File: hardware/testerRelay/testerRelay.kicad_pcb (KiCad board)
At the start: 2 copper layers, 100 x 70 mm, 12 parts, among them J21 relay, J22 relay, J70 transformer, J71 PM9808_L, J72 actuator, K10 HF115-005-2ZS4, K11 HF115-005-2ZS4, K12 HF115-005-2ZS4, K13 HF115-005-2ZS4, K14 HF115-005-2ZS4, K15 HF115-005-2ZS4, K16 HF115-005-2ZS4

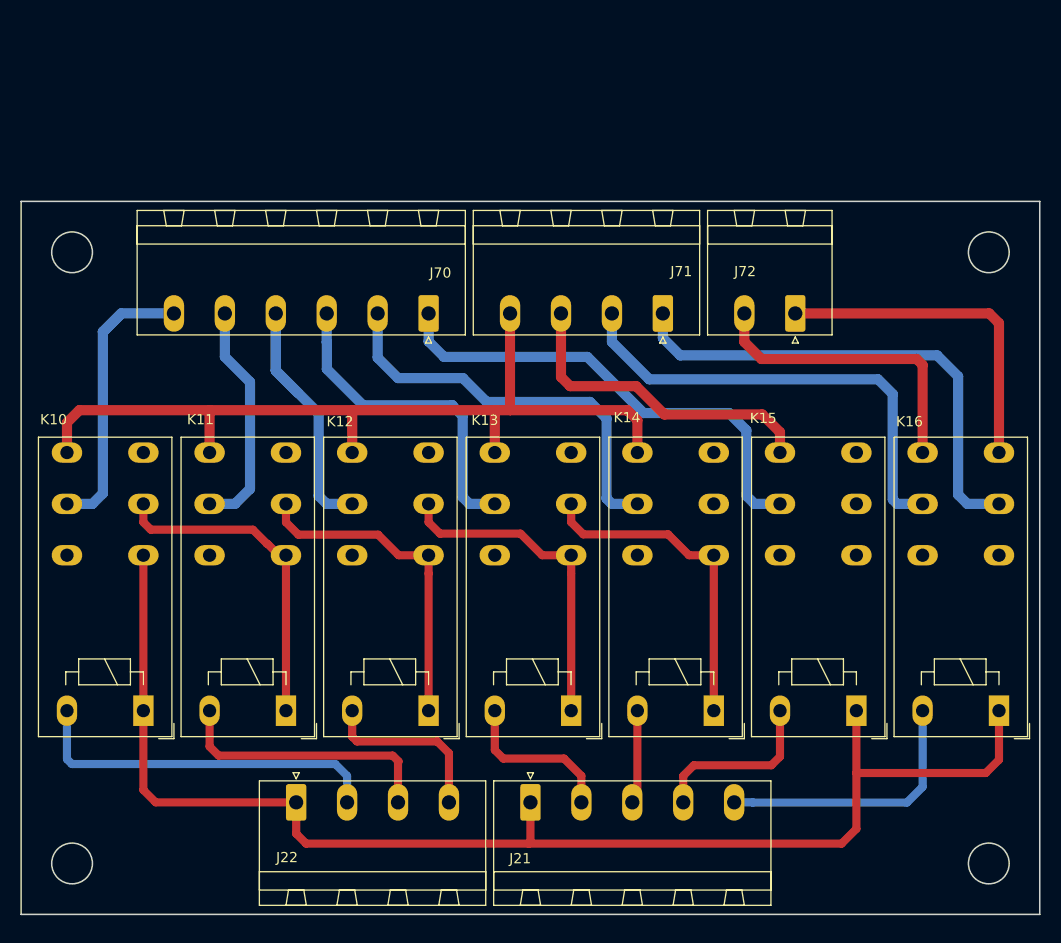
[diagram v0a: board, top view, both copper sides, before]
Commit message: adjustment line direction
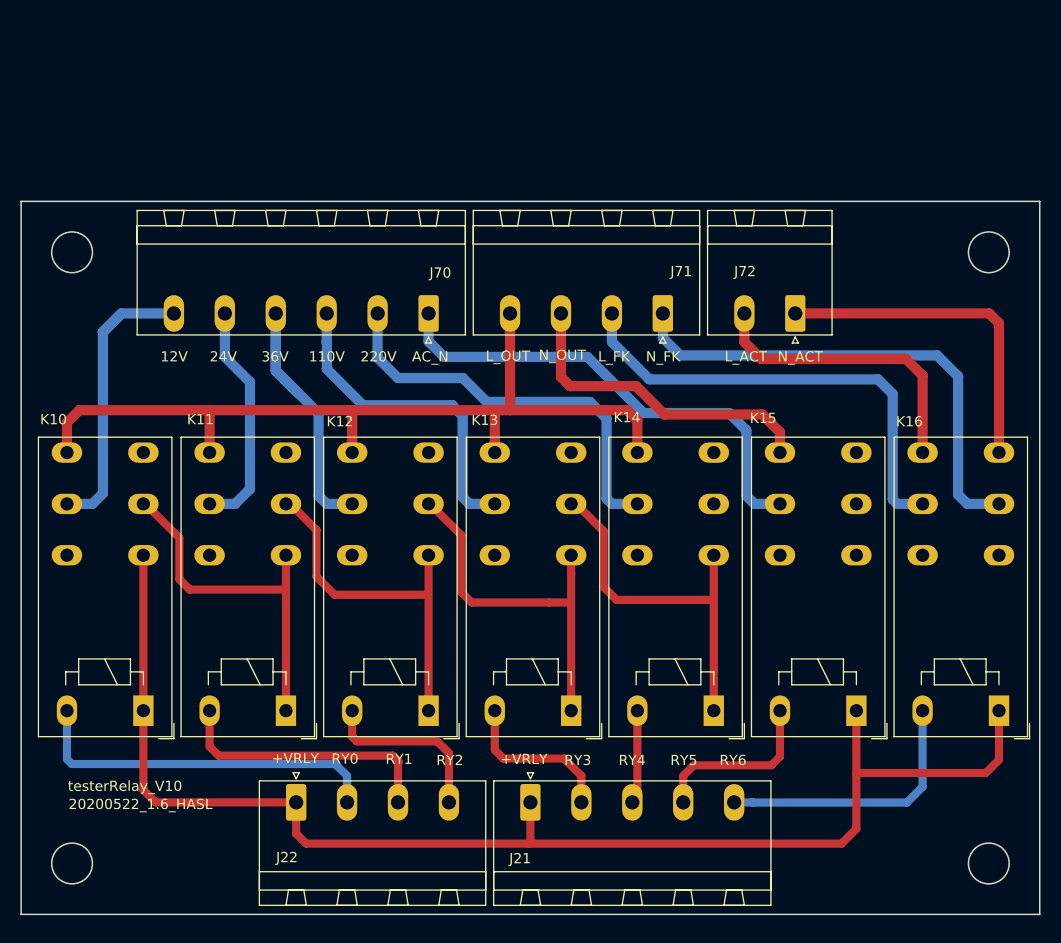
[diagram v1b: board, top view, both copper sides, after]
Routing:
- net /K13CV: track 32.4 -> 36.2 mm
- net /K14CV: track 32.4 -> 36.0 mm
- net /K12CV: track 32.4 -> 35.5 mm
- net /K11CV: track 32.4 -> 35.1 mm
- net /L_ACT: track 29.8 -> 29.2 mm
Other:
- board text added: "+VRLY"
- board text added: "110V"
- board text added: "12V"
- board text added: "20200522_1.6_HASL"
- board text added: "220V"
- board text added: "24V"
- board text added: "36V"
- board text added: "AC_N"
- board text added: "L_ACT"
- board text added: "L_FK"
- board text added: "L_OUT"
- board text added: "N_ACT"
- board text added: "N_FK"
- board text added: "N_OUT"
- board text added: "RY0"
- board text added: "RY1"
- board text added: "RY2"
- board text added: "RY3"
- board text added: "RY4"
- board text added: "RY5"
- board text added: "RY6"
- board text added: "testerRelay_V10"
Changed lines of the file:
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@@
   (general
     (thickness 1.6)
-    (drawings 8)
-    (tracks 181)
+    (drawings 31)
+    (tracks 179)
     (zones 0)
     (modules 12)
@@
     (pad_to_mask_clearance 0)
     (aux_axis_origin 0 0)
-    (visible_elements FFFFFF7F)
+    (visible_elements 7FFFFFFF)
     (pcbplotparams
       (layerselection 0x010fc_ffffffff)
@@
       (outputformat 1)
       (mirror false)
-      (drillshape 1)
+      (drillshape 0)
       (scaleselection 1)
-      (outputdirectory ""))
+      (outputdirectory "testerRelay_V10"))
   )
   (net 0 "")
@@
       (rotate (xyz 0 0 0))
     )
+  )
+  (gr_text 20200522_1.6_HASL (at 61.722 139.192) (layer F.SilkS)
+    (effects (font (size 1 1) (thickness 0.2)))
+  )
+  (gr_text testerRelay_V10 (at 60.198 137.414) (layer F.SilkS)
+    (effects (font (size 1 1) (thickness 0.2)))
+  )
+  (gr_text N_ACT (at 126.492 95.25) (layer F.SilkS)
+    (effects (font (size 1 1) (thickness 0.2)))
+  )
+  (gr_text L_ACT (at 121.158 95.25) (layer F.SilkS)
+    (effects (font (size 1 1) (thickness 0.2)))
+  )
+  (gr_text N_FK (at 113.03 95.25) (layer F.SilkS)
+    (effects (font (size 1 1) (thickness 0.2)))
+  )
+  (gr_text L_FK (at 108.204 95.25) (layer F.SilkS)
+    (effects (font (size 1 1) (thickness 0.2)))
+  )
+  (gr_text N_OUT (at 103.124 95.1) (layer F.SilkS)
+    (effects (font (size 1 1) (thickness 0.2)))
+  )
+  (gr_text L_OUT (at 97.79 95.19) (layer F.SilkS)
+    (effects (font (size 1 1) (thickness 0.2)))
+  )
+  (gr_text AC_N (at 90.17 95.25) (layer F.SilkS)
+    (effects (font (size 1 1) (thickness 0.2)))
+  )
+  (gr_text 220V (at 85.09 95.25) (layer F.SilkS)
+    (effects (font (size 1 1) (thickness 0.2)))
+  )
+  (gr_text 110V (at 80.01 95.25) (layer F.SilkS)
+    (effects (font (size 1 1) (thickness 0.2)))
+  )
+  (gr_text 36V (at 74.93 95.25) (layer F.SilkS)
+    (effects (font (size 1 1) (thickness 0.2)))
+  )
+  (gr_text 24V (at 69.85 95.25) (layer F.SilkS)
+    (effects (font (size 1 1) (thickness 0.2)))
+  )
+  (gr_text 12V (at 65.024 95.25) (layer F.SilkS)
+    (effects (font (size 1 1) (thickness 0.2)))
+  )
+  (gr_text RY6 (at 119.888 134.87) (layer F.SilkS)
+    (effects (font (size 1 1) (thickness 0.2)))
+  )
+  (gr_text RY5 (at 115.062 134.874) (layer F.SilkS)
+    (effects (font (size 1 1) (thickness 0.2)))
+  )
+  (gr_text RY4 (at 109.982 134.874) (layer F.SilkS)
+    (effects (font (size 1 1) (thickness 0.2)))
+  )
+  (gr_text RY3 (at 104.648 134.874) (layer F.SilkS)
+    (effects (font (size 1 1) (thickness 0.2)))
+  )
+  (gr_text +VRLY (at 99.36 134.77) (layer F.SilkS)
+    (effects (font (size 1 1) (thickness 0.2)))
+  )
+  (gr_text RY2 (at 92.09 134.88) (layer F.SilkS)
+    (effects (font (size 1 1) (thickness 0.2)))
+  )
+  (gr_text RY1 (at 87.1 134.76) (layer F.SilkS)
+    (effects (font (size 1 1) (thickness 0.2)))
+  )
+  (gr_text RY0 (at 81.79 134.74) (layer F.SilkS)
+    (effects (font (size 1 1) (thickness 0.2)))
+  )
+  (gr_text +VRLY (at 76.92 134.7) (layer F.SilkS)
+    (effects (font (size 1 1) (thickness 0.2)))
   )
   (gr_circle (center 55 85) (end 57 85) (layer Edge.Cuts) (width 0.15))
@@
   (segment (start 146 91.96) (end 146 104.66) (width 1) (layer F.Cu) (net 19))
   (segment (start 145.04 91) (end 146 91.96) (width 1) (layer F.Cu) (net 19))
-  (segment (start 122.67 95.47) (end 137.91 95.47) (width 1) (layer F.Cu) (net 20))
+  (segment (start 138.5 97.098) (end 138.5 104.66) (width 1) (layer F.Cu) (net 20))
+  (segment (start 122.67 95.47) (end 136.872 95.47) (width 1) (layer F.Cu) (net 20))
   (segment (start 121 91) (end 121 93.8) (width 1) (layer F.Cu) (net 20))
+  (segment (start 136.872 95.47) (end 138.5 97.098) (width 1) (layer F.Cu) (net 20))
   (segment (start 121 93.8) (end 122.67 95.47) (width 1) (layer F.Cu) (net 20))
-  (segment (start 138.5 96.06) (end 138.5 104.66) (width 1) (layer F.Cu) (net 20))
-  (segment (start 137.91 95.47) (end 138.5 96.06) (width 1) (layer F.Cu) (net 20))
+  (segment (start 62 109.7) (end 62.202 109.7) (width 0.8) (layer F.Cu) (net 21))
+  (segment (start 65.532 113.03) (end 65.532 117.094) (width 0.8) (layer F.Cu) (net 21))
+  (segment (start 62.202 109.7) (end 65.532 113.03) (width 0.8) (layer F.Cu) (net 21))
+  (segment (start 66.548 118.11) (end 75.946 118.11) (width 0.8) (layer F.Cu) (net 21))
+  (segment (start 65.532 117.094) (end 66.548 118.11) (width 0.8) (layer F.Cu) (net 21))
   (segment (start 76 114.74) (end 76 130) (width 0.8) (layer F.Cu) (net 21))
-  (segment (start 62 111.5) (end 62.73 112.23) (width 0.8) (layer F.Cu) (net 21))
-  (segment (start 62 109.7) (end 62 111.5) (width 0.8) (layer F.Cu) (net 21))
-  (segment (start 62.73 112.23) (end 72.75 112.23) (width 0.8) (layer F.Cu) (net 21))
-  (segment (start 72.75 112.23) (end 74.14 113.62) (width 0.8) (layer F.Cu) (net 21))
-  (segment (start 74.14 113.62) (end 74.19 113.62) (width 0.8) (layer F.Cu) (net 21))
-  (segment (start 75.31 114.74) (end 76 114.74) (width 0.8) (layer F.Cu) (net 21))
-  (segment (start 74.19 113.62) (end 75.31 114.74) (width 0.8) (layer F.Cu) (net 21))
-  (segment (start 85.04 112.72) (end 87.06 114.74) (width 0.8) (layer F.Cu) (net 26))
-  (segment (start 77.22 112.72) (end 85.04 112.72) (width 0.8) (layer F.Cu) (net 26))
-  (segment (start 87.06 114.74) (end 90 114.74) (width 0.8) (layer F.Cu) (net 26))
-  (segment (start 76 109.7) (end 76 111.5) (width 0.8) (layer F.Cu) (net 26))
-  (segment (start 76 111.5) (end 77.22 112.72) (width 0.8) (layer F.Cu) (net 26))
-  (segment (start 90 116.54) (end 90 130) (width 0.8) (layer F.Cu) (net 26))
-  (segment (start 90 114.74) (end 90 116.54) (width 0.8) (layer F.Cu) (net 26))
-  (segment (start 90 111.5) (end 91.12 112.62) (width 0.8) (layer F.Cu) (net 27))
-  (segment (start 90 109.7) (end 90 111.5) (width 0.8) (layer F.Cu) (net 27))
-  (segment (start 91.12 112.62) (end 99.03 112.62) (width 0.8) (layer F.Cu) (net 27))
-  (segment (start 101.15 114.74) (end 104 114.74) (width 0.8) (layer F.Cu) (net 27))
-  (segment (start 99.03 112.62) (end 101.15 114.74) (width 0.8) (layer F.Cu) (net 27))
+  (segment (start 76 109.7) (end 76.426 109.7) (width 0.8) (layer F.Cu) (net 26))
+  (segment (start 76.426 109.7) (end 78.994 112.268) (width 0.8) (layer F.Cu) (net 26))
+  (segment (start 78.994 112.268) (end 78.994 116.84) (width 0.8) (layer F.Cu) (net 26))
+  (segment (start 80.772 118.618) (end 89.916 118.618) (width 0.8) (layer F.Cu) (net 26))
+  (segment (start 78.994 116.84) (end 80.772 118.618) (width 0.8) (layer F.Cu) (net 26))
+  (segment (start 90 114.74) (end 90 130) (width 0.8) (layer F.Cu) (net 26))
   (segment (start 104 116.54) (end 104 130) (width 0.8) (layer F.Cu) (net 27))
   (segment (start 104 114.74) (end 104 116.54) (width 0.8) (layer F.Cu) (net 27))
-  (segment (start 104 111.5) (end 105.19 112.69) (width 0.8) (layer F.Cu) (net 32))
-  (segment (start 104 109.7) (end 104 111.5) (width 0.8) (layer F.Cu) (net 32))
-  (segment (start 105.19 112.69) (end 113.52 112.69) (width 0.8) (layer F.Cu) (net 32))
-  (segment (start 115.57 114.74) (end 118 114.74) (width 0.8) (layer F.Cu) (net 32))
-  (segment (start 113.52 112.69) (end 115.57 114.74) (width 0.8) (layer F.Cu) (net 32))
+  (segment (start 101.854 119.38) (end 103.632 119.38) (width 0.8) (layer F.Cu) (net 27))
+  (segment (start 90.142 109.7) (end 93.218 112.776) (width 0.8) (layer F.Cu) (net 27))
+  (segment (start 93.218 112.776) (end 93.218 118.364) (width 0.8) (layer F.Cu) (net 27))
+  (segment (start 94.234 119.38) (end 101.854 119.38) (width 0.8) (layer F.Cu) (net 27))
+  (segment (start 90 109.7) (end 90.142 109.7) (width 0.8) (layer F.Cu) (net 27))
+  (segment (start 93.218 118.364) (end 94.234 119.38) (width 0.8) (layer F.Cu) (net 27))
   (segment (start 118 114.74) (end 118 130) (width 0.8) (layer F.Cu) (net 32))
+  (segment (start 107.188 117.856) (end 108.458 119.126) (width 0.8) (layer F.Cu) (net 32))
+  (segment (start 107.188 112.388) (end 107.188 117.856) (width 0.8) (layer F.Cu) (net 32))
+  (segment (start 108.458 119.126) (end 117.602 119.126) (width 0.8) (layer F.Cu) (net 32))
+  (segment (start 104 109.7) (end 104.5 109.7) (width 0.8) (layer F.Cu) (net 32))
+  (segment (start 104.5 109.7) (end 107.188 112.388) (width 0.8) (layer F.Cu) (net 32))
 )

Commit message: 修改pcb文件，增加外壳支持
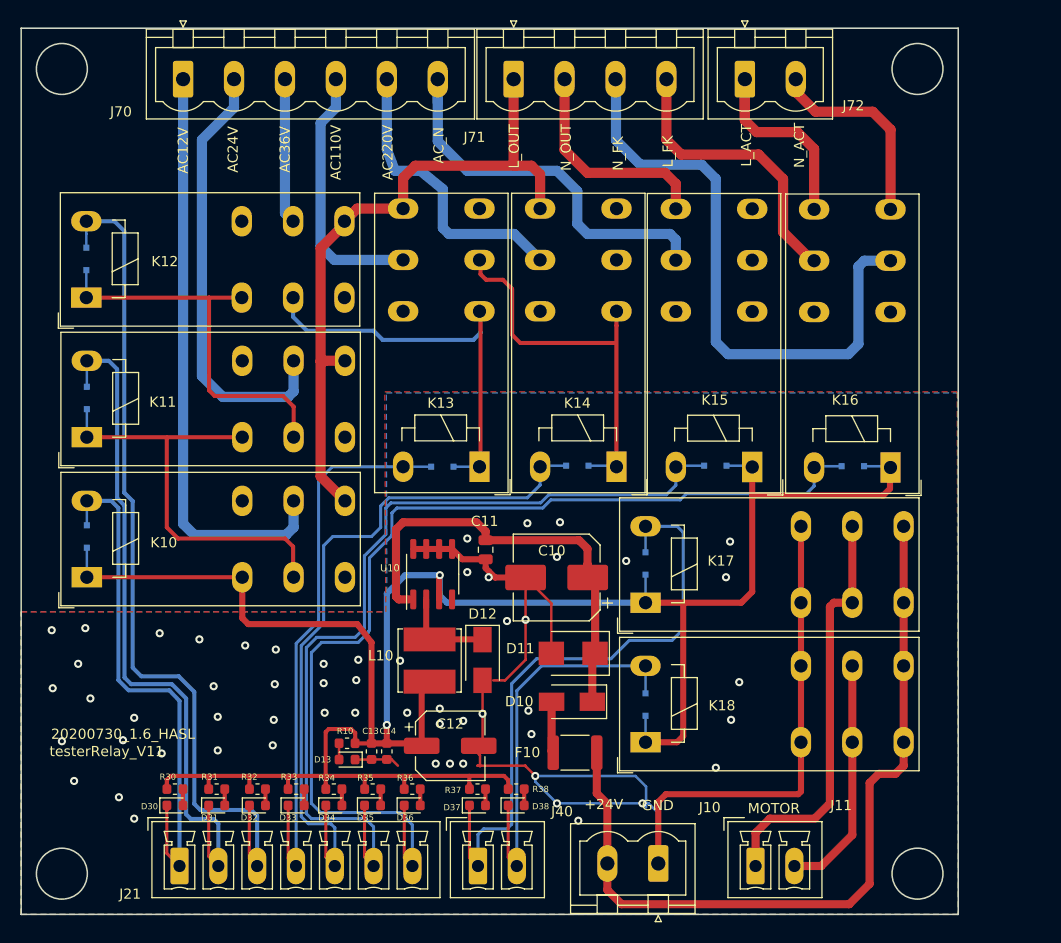
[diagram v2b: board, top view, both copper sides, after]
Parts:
- removed J22: relay, kicad_footprint_general:PhoenixContact_MSTBA_2,5_4-G_1x04_P5.00mm_Horizontal
- added C10: 47uF, kicad_footprint_general:CP_Elec_8x6.5, F.Cu at (102.6, 116.9)
- added C11: 1uF, kicad_footprint_general:C_0805_2012Metric, F.Cu at (95.6, 114.2)
- added C12: 220uF, kicad_footprint_general:CP_Elec_6.3x5.4, F.Cu at (92.1, 133.4)
- added C13: 1uF, kicad_footprint_general:C_0603_1608Metric, F.Cu at (84.4, 134.0)
- added C14: 100nF, kicad_footprint_general:C_0603_1608Metric, F.Cu at (85.9, 134.0)
- added D10: SS14, kicad_footprint_general:D_SMA, F.Cu at (104.1, 129.1)
- added D11: SMBJ28A, kicad_footprint_general:D_SMB, F.Cu at (104.2, 124.4)
- added D12: SS14, kicad_footprint_general:D_SMA, F.Cu at (95.3, 125.0)
- added D13: red, kicad_footprint_general:LED_0603_1608Metric, F.Cu at (82.0, 134.8)
- added D20: 1N4148, kicad_footprint_general:D_SOD-323F, B.Cu at (56.5, 112.9)
- added D21: 1N4148, kicad_footprint_general:D_SOD-323F, B.Cu at (56.5, 99.3)
- added D22: 1N4148, kicad_footprint_general:D_SOD-323F, B.Cu at (56.4, 85.7)
- added D23: 1N4148, kicad_footprint_general:D_SOD-323F, B.Cu at (91.3, 106.0)
- added D24: 1N4148, kicad_footprint_general:D_SOD-323F, B.Cu at (104.6, 106.0)
- added D25: 1N4148, kicad_footprint_general:D_SOD-323F, B.Cu at (118.2, 106.0)
- added D26: 1N4148, kicad_footprint_general:D_SOD-323F, B.Cu at (131.7, 106.0)
- added D27: 1N4148, kicad_footprint_general:D_SOD-323F, B.Cu at (111.3, 129.4)
- added D28: 1N4148, kicad_footprint_general:D_SOD-323F, B.Cu at (111.3, 115.5)
- added D30: red, kicad_footprint_general:LED_0603_1608Metric, F.Cu at (65.1, 139.3)
- added D31: red, kicad_footprint_general:LED_0603_1608Metric, F.Cu at (69.2, 139.3)
- added D32: red, kicad_footprint_general:LED_0603_1608Metric, F.Cu at (73.2, 139.3)
- added D33: red, kicad_footprint_general:LED_0603_1608Metric, F.Cu at (77.0, 139.3)
- added D34: red, kicad_footprint_general:LED_0603_1608Metric, F.Cu at (80.7, 139.3)
- added D35: red, kicad_footprint_general:LED_0603_1608Metric, F.Cu at (84.5, 139.3)
- added D36: red, kicad_footprint_general:LED_0603_1608Metric, F.Cu at (88.4, 139.3)
- added D37: red, kicad_footprint_general:LED_0603_1608Metric, F.Cu at (94.8, 139.3)
- added D38: red, kicad_footprint_general:LED_0603_1608Metric, F.Cu at (98.6, 139.3)
- added F10: 200mA, kicad_footprint_general:Fuse_1812_4532Metric, F.Cu at (104.4, 134.1)
- added J10: Power, kicad_footprint_general:PhoenixContact_MSTBVA_2,5_2-G_1x02_P5.00mm_Vertical, F.Cu at (112.5, 145.0)
- added J11: MOTOR, kicad_footprint_general:PhoenixContact_MCV_1,5_2-G-3.81_1x02_P3.81mm_Vertical, F.Cu at (122.1, 145.2)
- added J40: CK, kicad_footprint_general:PhoenixContact_MCV_1,5_2-G-3.81_1x02_P3.81mm_Vertical, F.Cu at (94.8, 145.2)
- added K17: HF115-005-2ZS4, kicad_footprint_general:Relay_DPDT_Schrack-RT2-FormC_RM5mm, F.Cu at (111.3, 119.4)
- added K18: HF115-005-2ZS4, kicad_footprint_general:Relay_DPDT_Schrack-RT2-FormC_RM5mm, F.Cu at (111.3, 133.1)
- added L10: 68uH, kicad_footprint_general:L_Bourns_SRN6045TA, F.Cu at (90.1, 125.1)
- added R10: 4.7k, kicad_footprint_general:R_0603_1608Metric, F.Cu at (82.0, 133.2)
- added R30: 4.7k, kicad_footprint_general:R_0603_1608Metric, F.Cu at (65.1, 137.7)
- added R31: 4.7k, kicad_footprint_general:R_0603_1608Metric, F.Cu at (69.2, 137.7)
- added R32: 4.7k, kicad_footprint_general:R_0603_1608Metric, F.Cu at (73.2, 137.7)
- added R33: 4.7k, kicad_footprint_general:R_0603_1608Metric, F.Cu at (77.0, 137.7)
- added R34: 4.7k, kicad_footprint_general:R_0603_1608Metric, F.Cu at (80.7, 137.7)
- added R35: 4.7k, kicad_footprint_general:R_0603_1608Metric, F.Cu at (84.5, 137.7)
- added R36: 4.7k, kicad_footprint_general:R_0603_1608Metric, F.Cu at (88.4, 137.7)
- added R37: 4.7k, kicad_footprint_general:R_0603_1608Metric, F.Cu at (94.8, 137.7)
- added R38: 4.7k, kicad_footprint_general:R_0603_1608Metric, F.Cu at (98.6, 137.7)
- added U10: XL1509, kicad_footprint_general:SOIC-8_3.9x4.9mm_P1.27mm, F.Cu at (90.4, 116.6)
- J21: value relay -> CK; footprint kicad_footprint_general:PhoenixContact_MSTBA_2,5_5-G_1x05_P5.00mm_Horizontal -> kicad_footprint_general:PhoenixContact_MCV_1,5_7-G-3.81_1x07_P3.81mm_Vertical
- J70: footprint kicad_footprint_general:PhoenixContact_MSTBA_2,5_6-G_1x06_P5.00mm_Horizontal -> kicad_footprint_general:PhoenixContact_MSTBVA_2,5_6-G_1x06_P5.00mm_Vertical
- J71: footprint kicad_footprint_general:PhoenixContact_MSTBA_2,5_4-G_1x04_P5.00mm_Horizontal -> kicad_footprint_general:PhoenixContact_MSTBVA_2,5_4-G_1x04_P5.00mm_Vertical
- J72: footprint kicad_footprint_general:PhoenixContact_MSTBA_2,5_2-G_1x02_P5.00mm_Horizontal -> kicad_footprint_general:PhoenixContact_MSTBVA_2,5_2-G_1x02_P5.00mm_Vertical
- moved K12 52.7 mm to (56.4, 89.5), turned to 0 degrees
- moved J21 35.0 mm to (65.5, 145.2)
- moved J70 33.3 mm to (65.9, 68.0), turned to 0 degrees
- moved K11 33.2 mm to (56.5, 103.2), turned to 0 degrees
- moved J71 27.3 mm to (98.3, 68.0), turned to 0 degrees
- moved K16 26.1 mm to (135.3, 106.1)
- moved K15 26.0 mm to (121.8, 106.1)
- moved K14 25.8 mm to (108.5, 106.0)
- moved K13 25.6 mm to (95.0, 106.0)
- moved J72 23.5 mm to (121.0, 68.0), turned to 0 degrees
- moved K10 14.2 mm to (56.5, 116.9), turned to 0 degrees
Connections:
- J21 pad 1: /+VRLY -> /CK0
- J21 pad 2: /C_CK3 -> /CK1
- J21 pad 3: /C_CK4 -> /CK2
- J21 pad 4: /C_CK5 -> /CK3
- J21 pad 5: /C_CK6 -> /CK4
- J70 pad 1: /AC_N -> /AC12V
- J70 pad 2: /AC220V -> /AC24V
- J70 pad 3: /AC110V -> /AC36V
- J70 pad 4: /AC36V -> /AC110V
- J70 pad 5: /AC24V -> /AC220V
- J70 pad 6: /AC12V -> /AC_N
- J71 pad 1: /N_FK -> /L_OUT
- J71 pad 2: /L_FK -> /N_OUT
- J71 pad 3: /N_OUT -> /N_FK
- J71 pad 4: /L_OUT -> /L_FK
- J72 pad 1: /N_ACT -> /L_ACT
- J72 pad 2: /L_ACT -> /N_ACT
- K10 pad 12: /+VRLY -> +5VD
- K10 pad A1: /+VRLY -> +5VD
- K10 pad A2: /C_CK0 -> /CK0
- K11 pad A2: /C_CK1 -> /CK1
- K12 pad A2: /C_CK2 -> /CK2
- K13 pad A2: /C_CK3 -> /CK3
- K14 pad A2: /C_CK4 -> /CK4
- K15 pad A1: /+VRLY -> +5VD
- K15 pad A2: /C_CK5 -> /CK5
- K16 pad A1: /+VRLY -> +5VD
- K16 pad A2: /C_CK6 -> /CK6
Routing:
- net +5VD: track 0.00 -> 224.5 mm, vias 0 -> 2
- net GND: track 0.00 -> 153.6 mm, vias 0 -> 57
- net /+VRLY: track 132.7 -> 0.00 mm
- net /CK6: track 0.00 -> 102.1 mm
- net /L_OUT: track 166.1 -> 67.4 mm
- net /CK5: track 0.00 -> 86.8 mm
- net /CK2: track 0.00 -> 85.8 mm
- net /VIN: track 0.00 -> 78.5 mm
- net /CK4: track 0.00 -> 70.7 mm
- net /CK1: track 0.00 -> 68.8 mm
- net /CK7: track 0.00 -> 62.0 mm
- net /CK3: track 0.00 -> 56.6 mm
- net /CK0: track 0.00 -> 52.2 mm
- net VDD: track 0.00 -> 44.1 mm
- net /M_2: track 0.00 -> 40.9 mm
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- added copper zone on B.Cu, net GND
- added copper zone on F.Cu, net GND
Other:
- board size 100 x 70 mm -> 92 x 87 mm
- board text added: "+24V"
- board text added: "20200730_1.6_HASL"
- board text added: "AC110V"
- board text added: "AC12V"
- board text added: "AC220V"
- board text added: "AC24V"
- board text added: "AC36V"
- board text added: "GND"
- board text added: "MOTOR"
- board text added: "testerRelay_V11"
- board text removed: "+VRLY"
- board text removed: "110V"
- board text removed: "12V"
- board text removed: "20200522_1.6_HASL"
- board text removed: "220V"
- board text removed: "24V"
- board text removed: "36V"
- board text removed: "RY0"
- board text removed: "RY1"
- board text removed: "RY2"
- board text removed: "RY3"
- board text removed: "RY4"
- board text removed: "RY5"
- board text removed: "RY6"
- board text removed: "testerRelay_V10"

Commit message: 增加曲线角度计算，pcb重新打样5pcs
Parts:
- added C15: 3.3nF, kicad_footprint_general:C_0603_1608Metric, F.Cu at (85.0, 126.2)
- added R11: 1k, kicad_footprint_general:R_0603_1608Metric, F.Cu at (85.0, 124.6)
- added R12: 3.6k, kicad_footprint_general:R_0603_1608Metric, F.Cu at (85.0, 127.8)
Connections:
- U10 pad 3: +5VD -> Net-(C15-Pad2)
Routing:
- net Net-(C15-Pad2): track 0.00 -> 17.1 mm, vias 0 -> 2
- net +5VD: track 224.5 -> 237.0 mm, vias 2 -> 1
- net GND: track 153.6 -> 159.0 mm, vias 57 -> 58
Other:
- board text added: "20201215_1.6_HASL"
- board text added: "testerRelay_V12"
- board text removed: "20200730_1.6_HASL"
- board text removed: "testerRelay_V11"
